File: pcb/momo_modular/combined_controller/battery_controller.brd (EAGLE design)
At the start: 31.7 x 33 mm, 34 parts, among them U1 XRP7659, U2 MAX1555, U3 MCP1702, U4 PIC24F16KA101-X_PSSOP, U5 FLASH8MSOP8

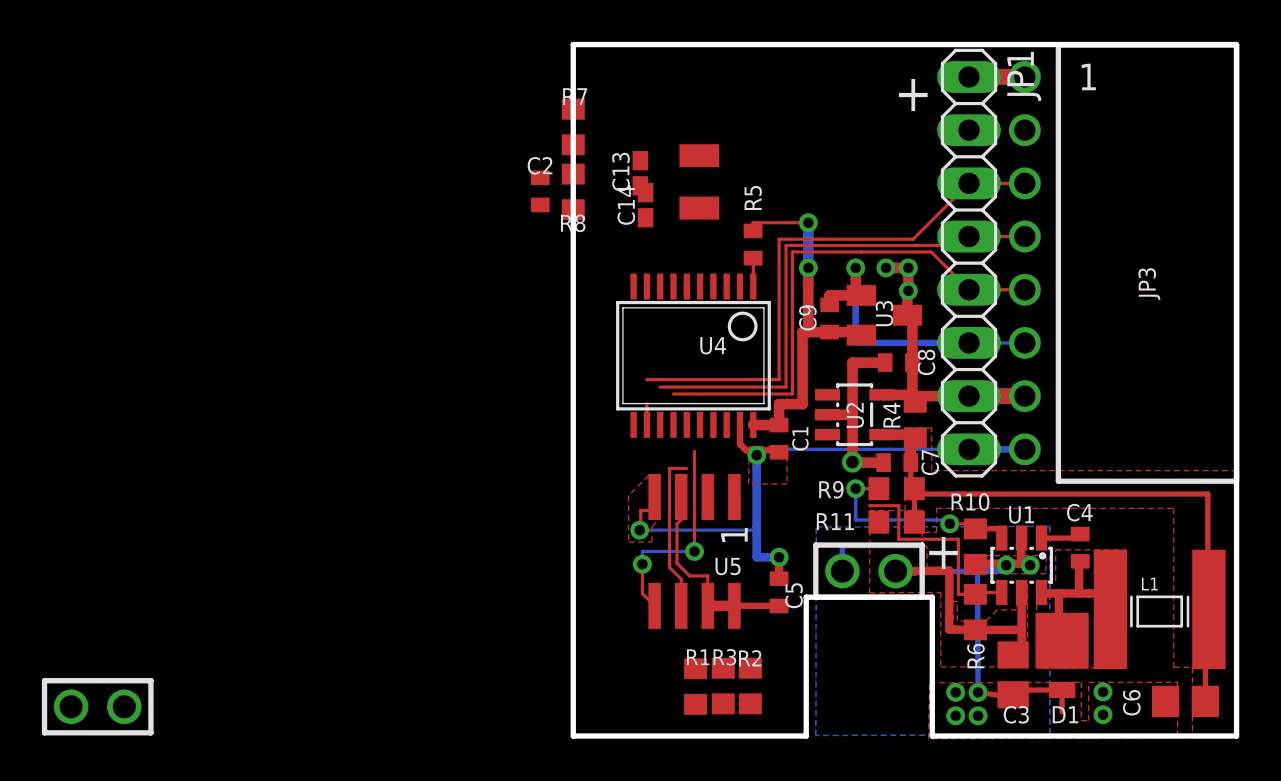
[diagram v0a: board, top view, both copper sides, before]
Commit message: Finished next version of hardware.  Working on automatic BOM generation for purchasing.
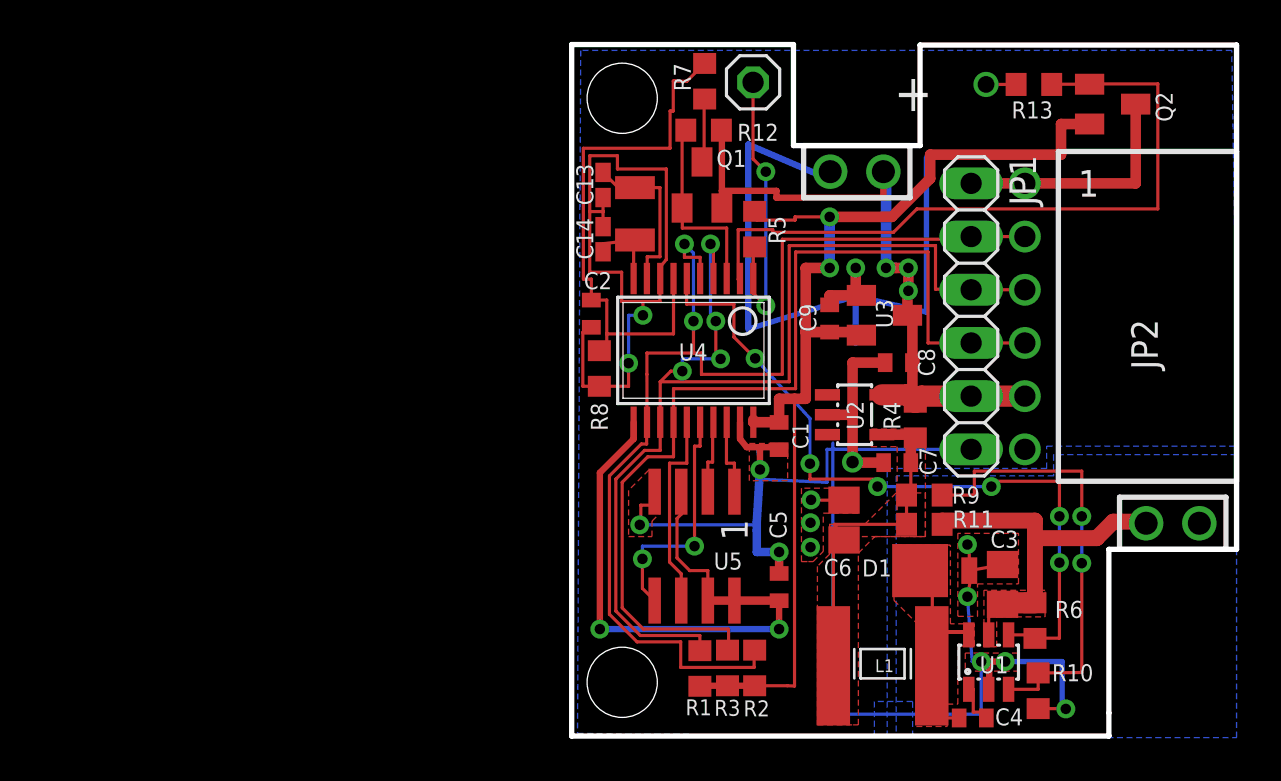
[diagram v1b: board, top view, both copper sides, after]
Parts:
- added JP2: MOMO-EDGE-6F, components:MOMO-EDGE-8F
- added Q1, Q2: P-MOSFET, components:SOT23
- added R12, R13: 100K, rcl:R0603
- JP1: value MOMO-VERT-8M -> MOMO-VERT-6M; device components:1X08 -> components:1X06
- JP3: value MOMO-EDGE-8F -> (none); device components:MOMO-EDGE-8F -> pinhead:1X01
- R10: value 9.7k -> 10k
- R5: value 10k -> 10K; device rcl:R0402 -> rcl:R0603
- R7, R8: value 500K -> 510K
- R9: value 50k -> 51k
- moved U$2 44.3 mm to (47.8, 39.0)
- moved C6 18.5 mm to (47.2, 22.4), turned to 90 degrees
- moved JP3 16.3 mm to (42.8, 43.3)
- moved U$1 14.7 mm to (62.9, 22.2)
- moved C4 9.61 mm to (53.3, 12.9), turned to 180 degrees
- moved L1 8.95 mm to (51.4, 15.4), turned to 180 degrees
- moved R8 8.52 mm to (35.5, 29.6)
- moved D1 7.57 mm to (50.8, 20.0), turned to 0 degrees
- moved R10 7.51 mm to (56.4, 14.2)
- moved R7 6.64 mm to (40.5, 43.3), turned to 270 degrees
- moved C2 6.33 mm to (35.1, 32.2)
- moved JP1 5.08 mm to (53.2, 29.6)
- moved U1 4.88 mm to (54.1, 15.6), turned to 0 degrees
- moved C3 4.35 mm to (54.7, 19.3), turned to 90 degrees
- moved XTAL1 3.43 mm to (37.2, 38.3)
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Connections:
- net N$6 renamed VBAT_SAMP
- net N$9 renamed BUCK_EN
- new net MEM_POW: C5.1, U4.11, U5.3, U5.7, U5.8
- new net N$3: Q1.3, R7.2
- new net SAMP_EN: Q1.1, R12.2, U4.3
- new net VCCIO: JP1.1, JP2.V28, Q2.3
- new net VCC_EN: Q2.1, R13.2, U4.2
- net +18V: now also U$1.1; no longer U$1.2
- net GND: now also JP1.7, JP2.GND, R13.1, U$1.2, U$2.2; no longer JP1.6, JP1.8, JP3.GND, JP3.PGND, U$1.1, U$2.1
- net ICLK: now also JP2.CLK, U4.5; no longer JP3.CLK
- net IDAT: now also JP2.DAT, U4.4; no longer JP3.DAT
- net IRQ: now also JP2.ARLM; no longer JP3.ARLM
- net N$15: now also JP3.1
- net V+: now also JP1.6, JP2.V4, Q1.2, R12.1, U$2.1; no longer JP1.7, JP3.V4., R7.2, U$2.2
- net VCCINT: now also Q2.2; no longer C5.1, JP1.1, JP3.V28, U5.3, U5.7, U5.8
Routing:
- net GND: track 83.9 -> 155.3 mm, vias 13 -> 16
- net VCC_EN: track 0.00 -> 34.2 mm
- net MEM_POW: track 0.00 -> 30.8 mm, vias 0 -> 2
- net IDAT: track 24.3 -> 54.9 mm, vias 0 -> 4
- net ICLK: track 26.9 -> 56.6 mm, vias 0 -> 2
- net VBAT_SAMP: track 0.17 -> 26.3 mm
- net BUCK_EN: track 10.6 -> 35.9 mm, vias 0 -> 6
- net VCCINT: track 30.5 -> 54.6 mm
- net IRQ: track 24.3 -> 46.4 mm
- net V+: track 15.9 -> 33.8 mm
- net N$5: track 30.2 -> 16.9 mm
- net N$15: track 1.50 -> 14.0 mm, vias 0 -> 2
- net VCCIO: track 0.00 -> 11.6 mm
- net N$10: track 10.5 -> 21.7 mm
- net SAMP_EN: track 0.00 -> 9.29 mm
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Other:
- board size 31.7 x 33 mm -> 31.8 x 33 mm
- board text removed: "XTAL1"

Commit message: Finished versions of core MoMo hardware along with python tools to autogenerate bill of materials files for each board.
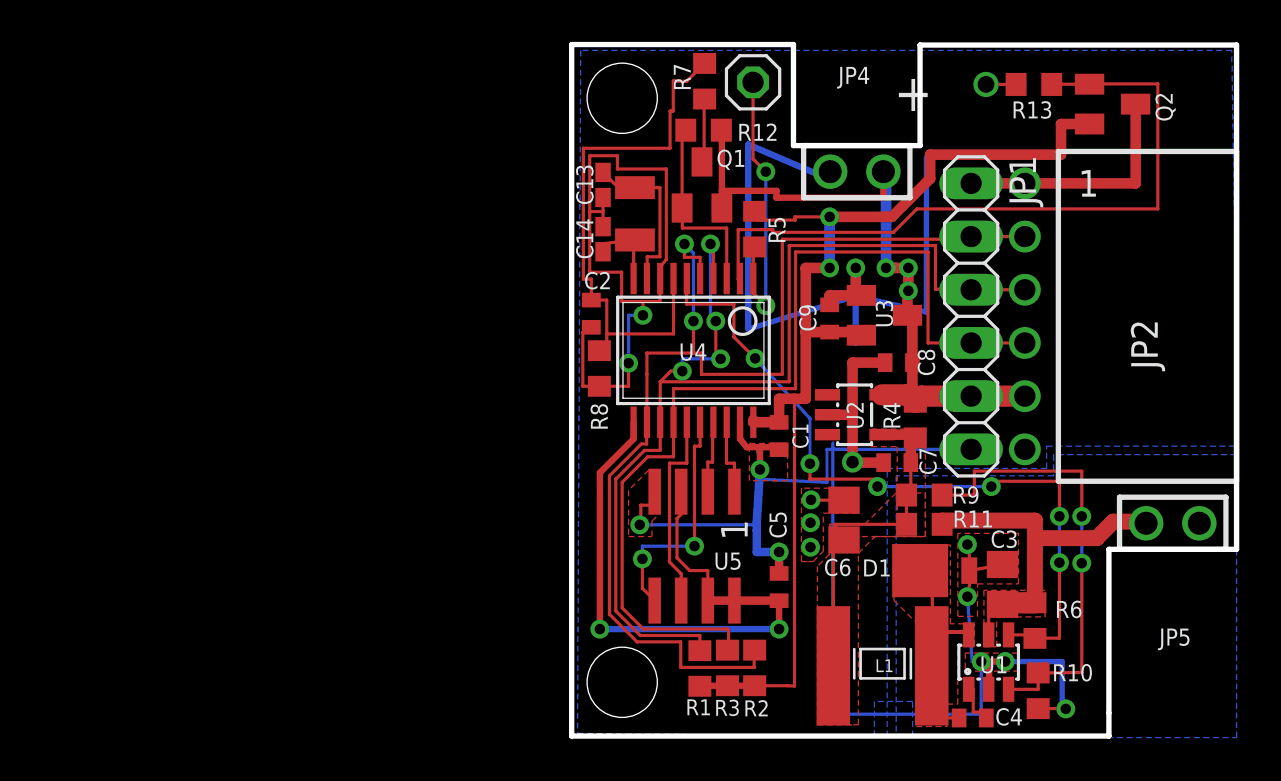
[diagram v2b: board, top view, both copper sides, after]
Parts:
- renumbered U$1 to JP5, U$2 to JP4
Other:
- board text removed: "JP4"
- board text removed: "JP5"
